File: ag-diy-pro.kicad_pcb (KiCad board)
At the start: 2 copper layers, 79.6 x 62.5 mm, 48 parts, among them U2 TPL5010, U3 SGP41-D-R4, U4 LM1117-3.3, U5 SHT4XI-DIGITAL, U6 ESP32-C3-MINI-1-N4

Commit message: Rev 2.0
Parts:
- removed C10, C12, C2, C8: 0.1uf, Capacitor_SMD:C_0603_1608Metric
- removed C11: 22uf / 10V, Capacitor_SMD:C_0603_1608Metric
- removed C7: 10uf / 25V, Capacitor_SMD:C_0603_1608Metric
- removed I2C1, I2C2, I2C3: Conn_01x04, Connector_PinSocket_2.54mm:PinSocket_1x04_P2.54mm_Vertical
- removed IO1, PM2: Conn_01x08_MountingPin, Connector_Molex:Molex_PicoBlade_53261-0871_1x08-1MP_P1.25mm_Horizontal
- removed the REF** at (111.9, 65.0)
- removed the REF** at (111.9, 98.0)
- removed the REF** at (156.9, 98.0)
- removed the REF** at (156.9, 65.0)
- removed S*2: Co2-S8, AG-PRO-Library:Co2-S8
- removed U4: LM1117-3.3, Package_TO_SOT_SMD:SOT-223-3_TabPin2
- added C14: 22uf, Capacitor_SMD:C_0603_1608Metric, F.Cu at (113.3, 62.6)
- added C15: 0.1uf, Capacitor_SMD:C_0603_1608Metric, F.Cu at (113.5, 67.0)
- added C22: 0.1uf, Capacitor_SMD:C_0603_1608Metric, F.Cu at (94.8, 43.0)
- added C23: 10uf, Capacitor_SMD:C_0603_1608Metric, F.Cu at (108.6, 62.7)
- added C24: 0.1uf, Capacitor_SMD:C_0603_1608Metric, F.Cu at (107.7, 65.1)
- added J1: BMV080, 503566-1302:5035661302, F.Cu at (119.0, 43.9)
- added J2: Conn_01x08, ZAir:S12, F.Cu at (105.2, 43.7)
- added J3: Pogo1, Connector_PinHeader_2.54mm:PinHeader_1x05_P2.54mm_Vertical, F.Cu at (78.8, 50.1)
- added J4: Pogo2, Connector_PinHeader_2.54mm:PinHeader_1x05_P2.54mm_Vertical, F.Cu at (96.9, 31.8)
- added J5: Pogo3, Connector_PinHeader_2.54mm:PinHeader_1x05_P2.54mm_Vertical, F.Cu at (125.2, 49.8)
- added L1: 2.2uH, Inductor_SMD:L_0603_1608Metric, F.Cu at (111.7, 62.6)
- added R18: 10k, Resistor_SMD:R_0603_1608Metric, F.Cu at (108.5, 67.4)
- added R20: 33.2k, Resistor_SMD:R_0603_1608Metric, F.Cu at (111.6, 70.0)
- added R9: 10k, Resistor_SMD:R_0603_1608Metric, F.Cu at (110.0, 70.0)
- added U1: TPS564201, Package_TO_SOT_SMD:SOT-23-6, F.Cu at (111.0, 66.3)
- C13: value 0.1uf -> 22uf
- C17: value 0.1uf -> 10uf
- C18: value 0.1uf -> 2uf
- USB1: footprint AG-PRO-Library:918-418K2022Y40000 -> Connector_USB:USB_C_Receptacle_Molex_105450-0101
- moved C21 49.5 mm to (112.8, 32.3), turned to 180 degrees
- moved R16 48.1 mm to (87.7, 48.7), turned to 90 degrees
- moved U3 43.5 mm to (116.1, 33.1), turned to 180 degrees
- moved R17 42.9 mm to (89.2, 48.7)
- moved R15 42.7 mm to (116.4, 35.4), turned to 180 degrees
- moved R8 41.5 mm to (123.9, 34.8), turned to 0 degrees
- moved C18 40.4 mm to (116.9, 44.0), turned to -90 degrees
- moved U2 37.3 mm to (123.3, 37.4), turned to 0 degrees
- moved C20 37.1 mm to (119.6, 33.9), turned to 0 degrees
- moved C4 36.5 mm to (119.7, 36.6), turned to 0 degrees
- moved C13 36.5 mm to (114.9, 62.6)
- moved R5 30.9 mm to (119.7, 38.1), turned to 180 degrees
- moved C17 29.0 mm to (110.2, 62.6), turned to 90 degrees
- moved REF** 28.6 mm to (105.1, 43.7)
- moved Boot1 24.4 mm to (98.2, 61.1)
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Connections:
- C13 pad 1: +5V -> +3.3V
- U6 pad 12: /RX_2_PMS -> /IRQ
- U6 pad 13: /TX_2_PMS -> /IO1
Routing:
- net GND: track 163.9 -> 335.9 mm, vias 150 -> 224
- net +5V: track 129.6 -> 10.7 mm, vias 4 -> 0
- net /SDA: track 170.1 -> 122.0 mm, vias 6 -> 7
- net /EN: track 53.7 -> 96.4 mm, vias 0 -> 4
- net Net-(F1-Pad2): track 54.0 -> 12.9 mm, vias 2 -> 0
- net /IRQ: track 0.00 -> 39.5 mm, vias 0 -> 4
- net /IO1: track 0.00 -> 38.0 mm, vias 0 -> 2
- net +3.3V: track 253.5 -> 215.9 mm, vias 11 -> 6
- net /RX_1_PMS: track 63.1 -> 25.8 mm
- net /SCL: track 166.8 -> 129.6 mm, vias 6 -> 10
- net /TX_1_PMS: track 66.1 -> 29.1 mm, vias 0 -> 1
- net /WD_RST: track 14.4 -> 46.3 mm
- net /IO5: track 26.1 -> 51.5 mm, vias 2 -> 4
- net /IO3: track 31.3 -> 52.8 mm
- net /BOOT: track 47.4 -> 26.9 mm
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- removed copper zone on F.Cu, net +3.3V
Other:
- board size 79.6 x 62.5 mm -> 50.3 x 50.3 mm
- board text removed: "3.3V GND SCL SDA"
- board text removed: "5V GND 3.3V IO5 IO4 IO3 SCL SDA"
- board text removed: "5V GND NC TX RX NC NC NC"
- board text removed: "BME"
- board text removed: "Boot SW"
- board text removed: "En"
- board text removed: "PMS"

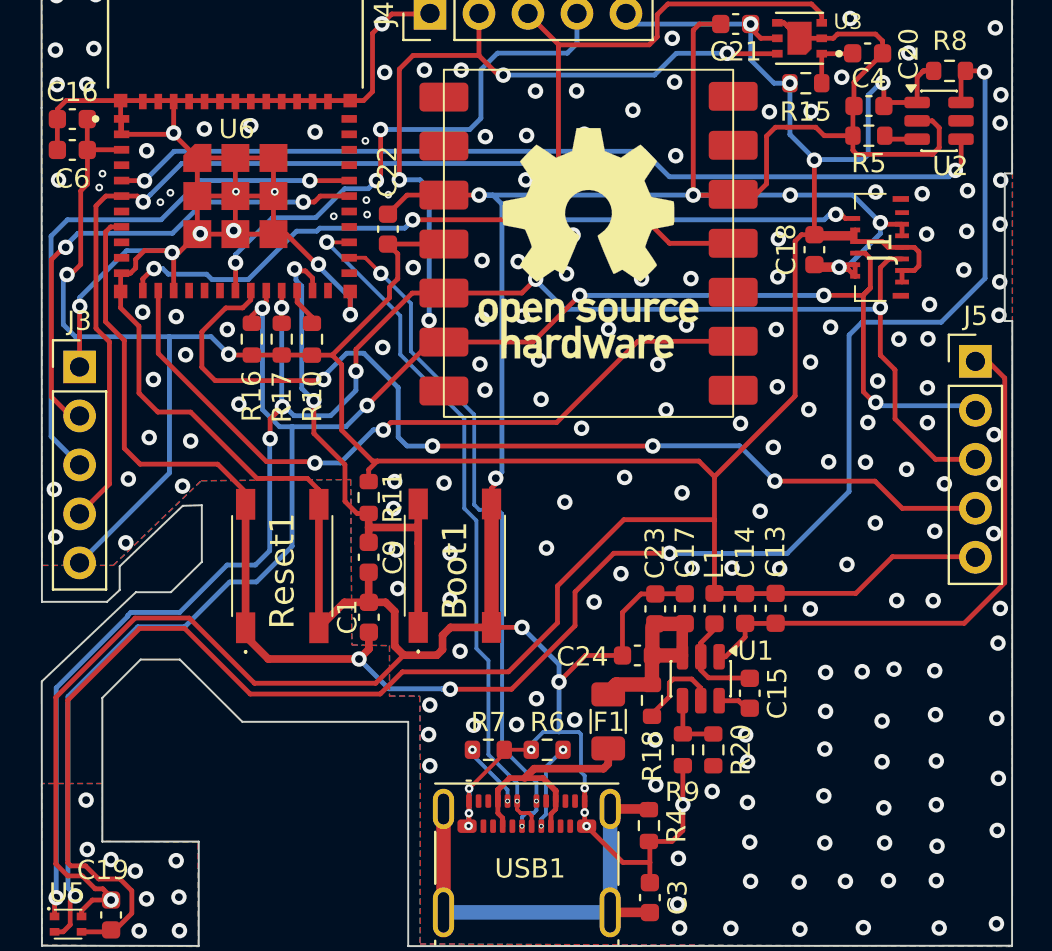
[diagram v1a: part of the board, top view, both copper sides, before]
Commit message: Upgraded tracks
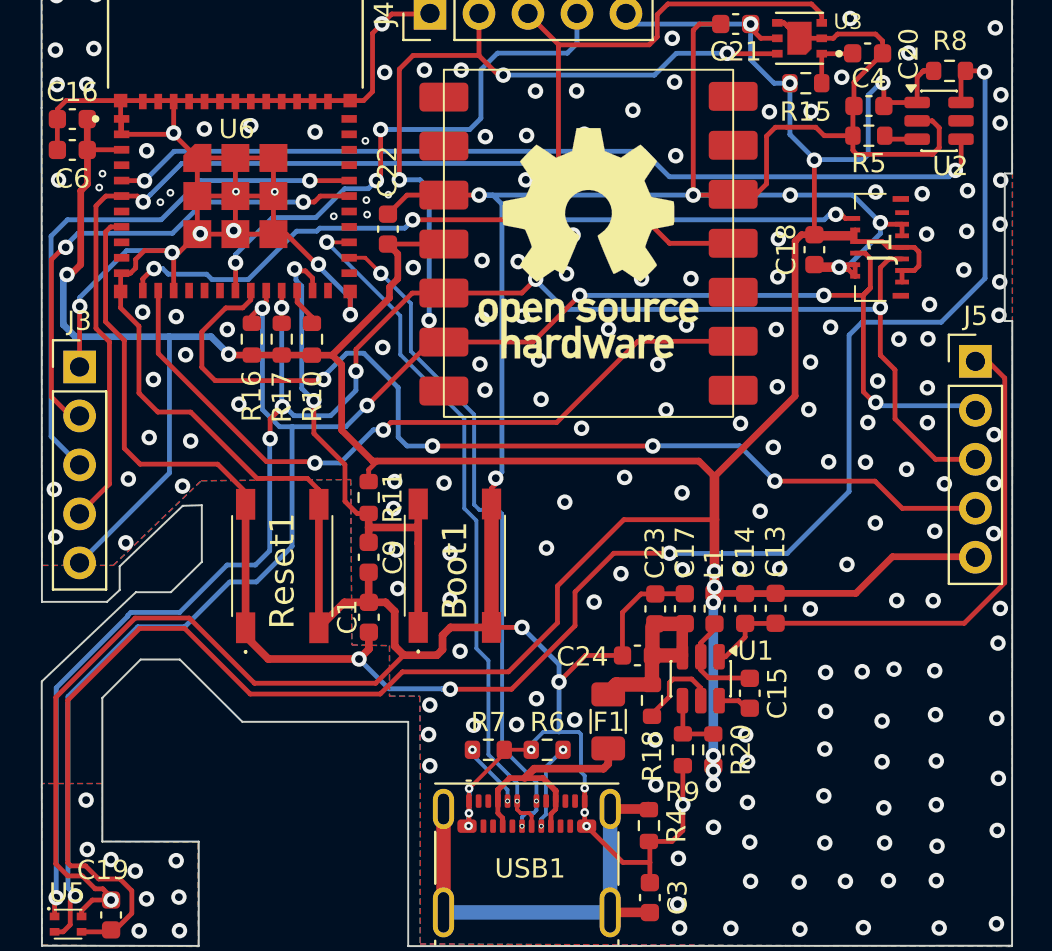
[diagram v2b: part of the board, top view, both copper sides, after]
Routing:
- net +3.3V: track 215.9 -> 226.9 mm, vias 6 -> 12
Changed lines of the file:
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@@
 		(start 114.86 61.85)
 		(end 119.02 61.85)
-		(width 0.25)
+		(width 0.35)
 		(layer "F.Cu")
 		(net "+3.3V")
@@
 		(start 90.82 49.5)
 		(end 91.87 49.5)
-		(width 0.25)
+		(width 0.35)
 		(layer "F.Cu")
 		(net "+3.3V")
@@
 		(start 87.7 49.495)
 		(end 86.545 49.495)
-		(width 0.25)
+		(width 0.35)
 		(layer "F.Cu")
 		(net "+3.3V")
@@
 		(start 111.69 55.8)
 		(end 115.87 51.62)
-		(width 0.25)
+		(width 0.35)
 		(layer "F.Cu")
 		(net "+3.3V")
@@
 		(start 93.96 54.99)
 		(end 92.36 53.39)
-		(width 0.25)
+		(width 0.35)
 		(layer "F.Cu")
 		(net "+3.3V")
@@
 		(start 92.36 49.99)
 		(end 91.87 49.5)
-		(width 0.25)
+		(width 0.35)
 		(layer "F.Cu")
 		(net "+3.3V")
@@
 		(start 110.88 54.99)
 		(end 94.21 54.99)
-		(width 0.25)
+		(width 0.35)
 		(layer "F.Cu")
 		(net "+3.3V")
@@
 		(start 111.69 58.03)
 		(end 111.69 55.8)
-		(width 0.25)
+		(width 0.5)
 		(layer "F.Cu")
 		(net "+3.3V")
@@
 	)
 	(segment
+		(start 111.69 60.7)
+		(end 111.69 58.03)
+		(width 0.5)
+		(layer "F.Cu")
+		(net "+3.3V")
+	)
+	(segment
 		(start 79.18 40.63)
 		(end 79.18 38.87)
-		(width 0.25)
+		(width 0.35)
 		(layer "F.Cu")
 		(net "+3.3V")
@@
 		(start 113.28 61.86)
 		(end 114.85 61.86)
-		(width 0.25)
+		(width 0.35)
 		(layer "F.Cu")
 		(net "+3.3V")
@@
 		(start 111.69 55.8)
 		(end 110.88 54.99)
-		(width 0.25)
+		(width 0.35)
 		(layer "F.Cu")
 		(net "+3.3V")
@@
 		(start 116.205 43.255)
 		(end 116.87 43.255)
-		(width 0.25)
+		(width 0.35)
 		(layer "F.Cu")
 		(net "+3.3V")
@@
 		(start 78.12 45.32)
 		(end 78.31 45.32)
-		(width 0.25)
+		(width 0.35)
 		(layer "F.Cu")
 		(net "+3.3V")
@@
 		(start 78.83 40.98)
 		(end 79.18 40.63)
-		(width 0.25)
+		(width 0.35)
 		(layer "F.Cu")
 		(net "+3.3V")
@@
 		(start 111.69 61.8525)
 		(end 113.2725 61.8525)
-		(width 0.25)
+		(width 0.35)
 		(layer "F.Cu")
 		(net "+3.3V")
@@
 	)
 	(segment
+		(start 111.69 61.52)
+		(end 111.69 60.7)
+		(width 0.5)
+		(layer "F.Cu")
+		(net "+3.3V")
+	)
+	(segment
 		(start 122.1975 36.4)
 		(end 120.6525 36.4)
@@
 		(start 91.87 49.5)
 		(end 94.84 46.53)
-		(width 0.25)
+		(width 0.35)
 		(layer "F.Cu")
 		(net "+3.3V")
@@
 		(start 78.83 44.8)
 		(end 78.83 40.98)
-		(width 0.25)
+		(width 0.35)
 		(layer "F.Cu")
 		(net "+3.3V")
@@
 		(start 79.17 37.26)
 		(end 79.17 38.86)
-		(width 0.25)
+		(width 0.35)
 		(layer "F.Cu")
 		(net "+3.3V")
@@
 		(start 94.21 54.99)
 		(end 93.96 54.99)
-		(width 0.25)
+		(width 0.35)
 		(layer "F.Cu")
 		(net "+3.3V")
@@
 		(start 95.27 45.54)
 		(end 95.27 44.25)
-		(width 0.25)
+		(width 0.35)
 		(layer "F.Cu")
 		(net "+3.3V")
@@
 		(start 95.27 44.25)
 		(end 94.76 43.74)
-		(width 0.25)
+		(width 0.35)
 		(layer "F.Cu")
 		(net "+3.3V")
@@
 		(start 115.87 43.59)
 		(end 116.205 43.255)
-		(width 0.25)
+		(width 0.35)
 		(layer "F.Cu")
 		(net "+3.3V")
@@
 	(segment
 		(start 111.69 61.8525)
-		(end 111.69 58.03)
-		(width 0.25)
+		(end 111.69 61.52)
+		(width 0.5)
 		(layer "F.Cu")
 		(net "+3.3V")
@@
 		(start 94.84 45.97)
 		(end 95.27 45.54)
-		(width 0.25)
+		(width 0.35)
 		(layer "F.Cu")
 		(net "+3.3V")
@@
 		(start 125.19 59.95)
 		(end 125.22 59.98)
-		(width 0.25)
+		(width 0.35)
 		(layer "F.Cu")
 		(net "+3.3V")
@@
 		(start 94.84 46.53)
 		(end 94.84 45.97)
-		(width 0.25)
+		(width 0.35)
 		(layer "F.Cu")
 		(net "+3.3V")
@@
 		(start 87.7 49.495)
 		(end 90.815 49.495)
-		(width 0.25)
+		(width 0.35)
 		(layer "F.Cu")
 		(net "+3.3V")
@@
 		(start 78.31 45.32)
 		(end 78.83 44.8)
-		(width 0.25)
+		(width 0.35)
 		(layer "F.Cu")
 		(net "+3.3V")
@@
 		(start 119.02 61.85)
 		(end 120.92 59.95)
-		(width 0.25)
+		(width 0.35)
 		(layer "F.Cu")
 		(net "+3.3V")
@@
 		(start 120.92 59.95)
 		(end 125.19 59.95)
-		(width 0.25)
+		(width 0.35)
 		(layer "F.Cu")
 		(net "+3.3V")
@@
 		(start 92.36 53.39)
 		(end 92.36 49.99)
-		(width 0.25)
+		(width 0.35)
 		(layer "F.Cu")
 		(net "+3.3V")
@@
 		(start 115.87 51.62)
 		(end 115.87 43.59)
-		(width 0.25)
+		(width 0.35)
 		(layer "F.Cu")
 		(net "+3.3V")
@@
 	)
 	(via
+		(at 111.63 62.32)
+		(size 0.8)
+		(drill 0.4)
+		(layers "F.Cu" "B.Cu")
+		(net "+3.3V")
+	)
+	(via
 		(at 113.565 32.33)
 		(size 0.8)
@@
 	)
 	(via
+		(at 111.69 60.7)
+		(size 0.8)
+		(drill 0.4)
+		(layers "F.Cu" "B.Cu")
+		(net "+3.3V")
+	)
+	(via
 		(at 115.6 35.4)
 		(size 0.8)
@@
 	)
 	(via
+		(at 111.63 70.27)
+		(size 0.8)
+		(drill 0.4)
+		(layers "F.Cu" "B.Cu")
+		(net "+3.3V")
+	)
+	(via
 		(at 116.87 39.39)
 		(size 0.8)
@@
 	)
 	(via
+		(at 111.63 71.76)
+		(size 0.8)
+		(drill 0.4)
+		(layers "F.Cu" "B.Cu")
+		(net "+3.3V")
+	)
+	(via
+		(at 111.63 71.04)
+		(size 0.8)
+		(drill 0.4)
+		(layers "F.Cu" "B.Cu")
+		(net "+3.3V")
+	)
+	(via
+		(at 111.69 61.52)
+		(size 0.8)
+		(drill 0.4)
+		(layers "F.Cu" "B.Cu")
+		(net "+3.3V")
+	)
+	(via
 		(at 78.12 45.32)
 		(size 0.8)
@@
 		(start 78.12 45.33)
 		(end 77.93 45.52)
-		(width 0.25)
+		(width 0.35)
+		(layer "B.Cu")
+		(net "+3.3V")
+	)
+	(segment
+		(start 111.63 71.04)
+		(end 111.63 70.27)
+		(width 0.5)
 		(layer "B.Cu")
 		(net "+3.3V")
@@
 		(start 77.93 47.92)
 		(end 78.55 48.54)
-		(width 0.25)
+		(width 0.35)
 		(layer "B.Cu")
 		(net "+3.3V")
@@
 	)
 	(segment
+		(start 111.63 71.04)
+		(end 111.63 71.76)
+		(width 0.5)
+		(layer "B.Cu")
+		(net "+3.3V")
+	)
+	(segment
 		(start 113.565 32.33)
 		(end 107.62 32.33)
@@
 	)
 	(segment
+		(start 111.63 62.32)
+		(end 111.63 61.58)
+		(width 0.5)
+		(layer "B.Cu")
+		(net "+3.3V")
+	)
+	(segment
+		(start 111.68 61.51)
+		(end 111.68 60.8)
+		(width 0.5)
+		(layer "B.Cu")
+		(net "+3.3V")
+	)
+	(segment
 		(start 107.62 32.33)
 		(end 107.1 31.81)
@@
 		(start 78.12 45.32)
 		(end 78.12 45.33)
-		(width 0.25)
+		(width 0.35)
+		(layer "B.Cu")
+		(net "+3.3V")
+	)
+	(segment
+		(start 111.69 61.52)
+		(end 111.68 61.51)
+		(width 0.5)
 		(layer "B.Cu")
 		(net "+3.3V")
@@
 		(start 78.55 48.54)
 		(end 83.42 48.54)
-		(width 0.25)
+		(width 0.35)
 		(layer "B.Cu")
 		(net "+3.3V")
@@
 	)
 	(segment
+		(start 111.63 61.58)
+		(end 111.69 61.52)
+		(width 0.5)
+		(layer "B.Cu")
+		(net "+3.3V")
+	)
+	(segment
 		(start 77.93 45.52)
 		(end 77.93 47.92)
-		(width 0.25)
+		(width 0.35)
 		(layer "B.Cu")
 		(net "+3.3V")
@@
 		(start 83.42 48.54)
 		(end 85.59 48.54)
-		(width 0.25)
+		(width 0.35)
 		(layer "B.Cu")
 		(net "+3.3V")
@@
 		(start 85.59 48.54)
 		(end 86.5 49.45)
-		(width 0.25)
+		(width 0.35)
 		(layer "B.Cu")
 		(net "+3.3V")
@@
 	)
 	(segment
+		(start 111.63 70.27)
+		(end 111.63 62.32)
+		(width 0.5)
+		(layer "B.Cu")
+		(net "+3.3V")
+	)
+	(segment
 		(start 80.9 45.3)
 		(end 80.95 45.25)
@@
 	)
 	(via
-		(at 112.6 60.54)
+		(at 113 60.58)
 		(size 0.8)
 		(drill 0.4)
@@
 	)
 	(via
-		(at 110.53 60.55)
+		(at 110.03 60.63)
 		(size 0.8)
 		(drill 0.4)
@@
 	)
 	(via
-		(at 111.57 72.12)
+		(at 111.64 73.98)
 		(size 0.8)
 		(drill 0.4)

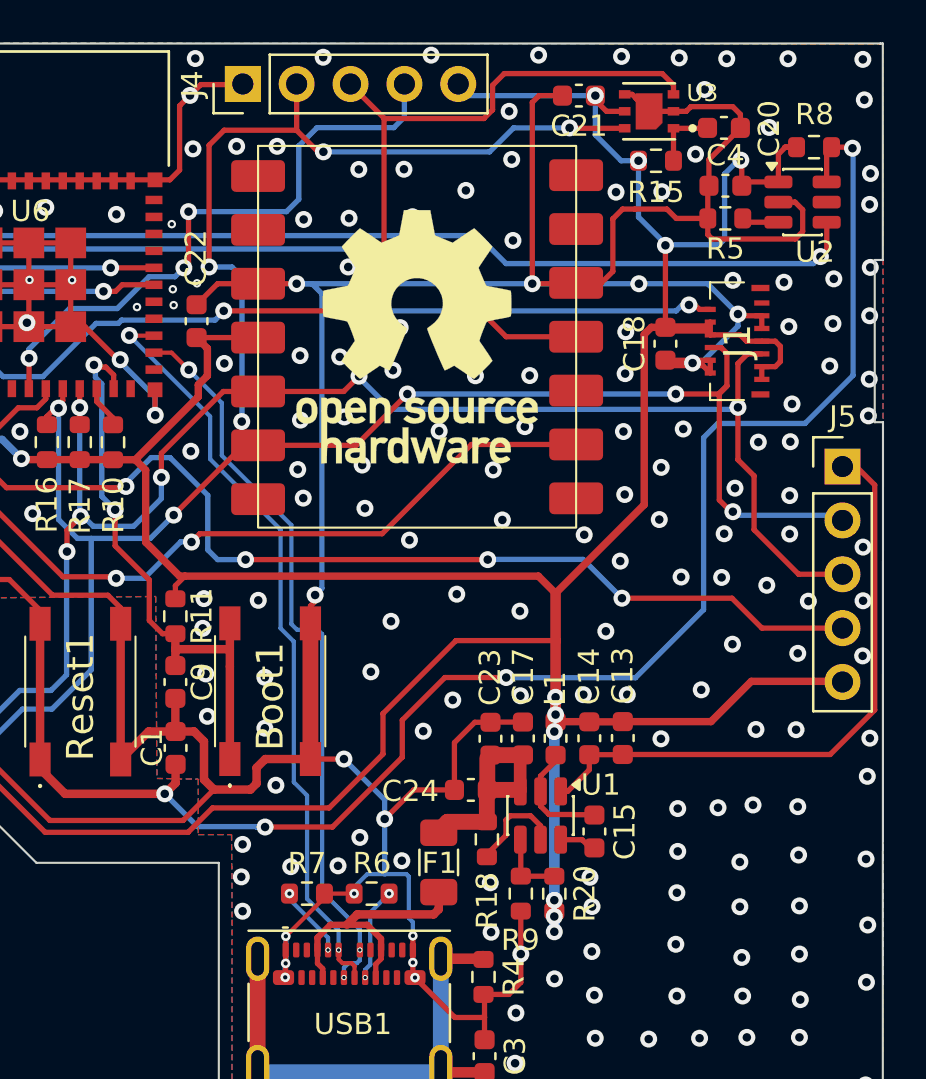
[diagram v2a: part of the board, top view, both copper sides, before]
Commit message: Wider tracks
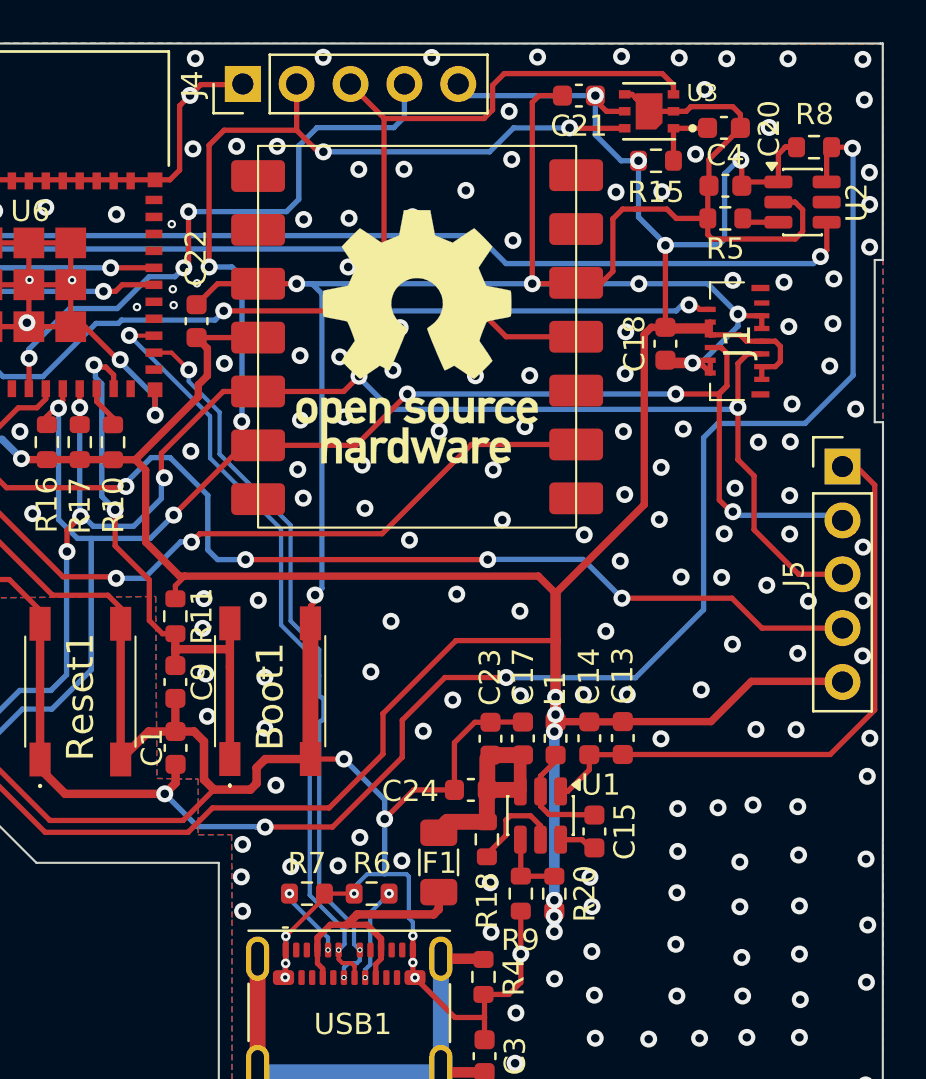
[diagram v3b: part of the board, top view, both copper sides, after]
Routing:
- net GND: vias 224 -> 222
